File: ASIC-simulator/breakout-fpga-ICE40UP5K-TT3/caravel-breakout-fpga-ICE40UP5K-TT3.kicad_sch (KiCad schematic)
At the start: 65 parts, among them CON1 REF-182665-01, CON2 REF-182665-01, J15 USB4500-03-0-A_REVA, U1 AP2112K-3.3, U2 AP2112K-1.2, U2 ICE40UP5K-SG48ITR, U5 W25Q32JVSSIM, X1 20MHz

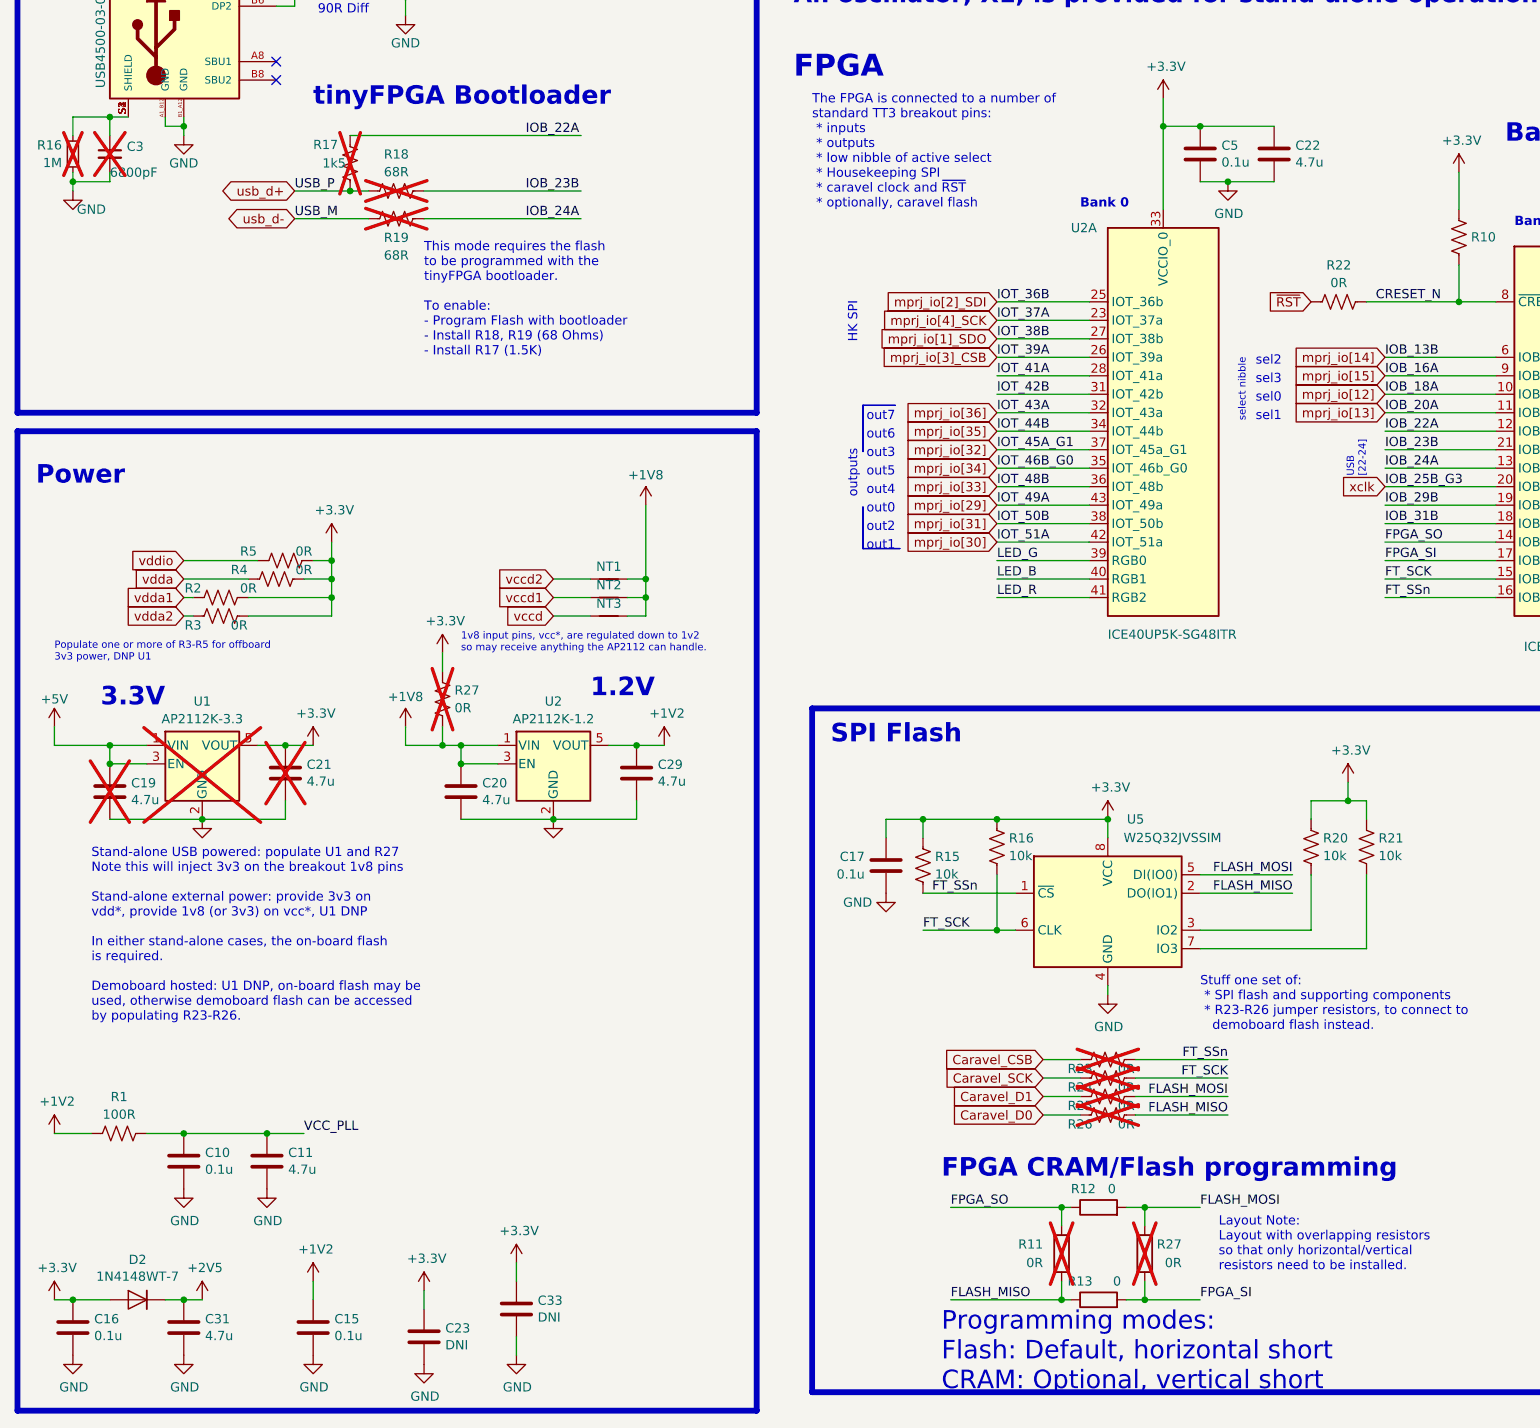
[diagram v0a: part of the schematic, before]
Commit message: ICE40UP5K TT3 breakout, BOM tweaks pre-PCBA first run
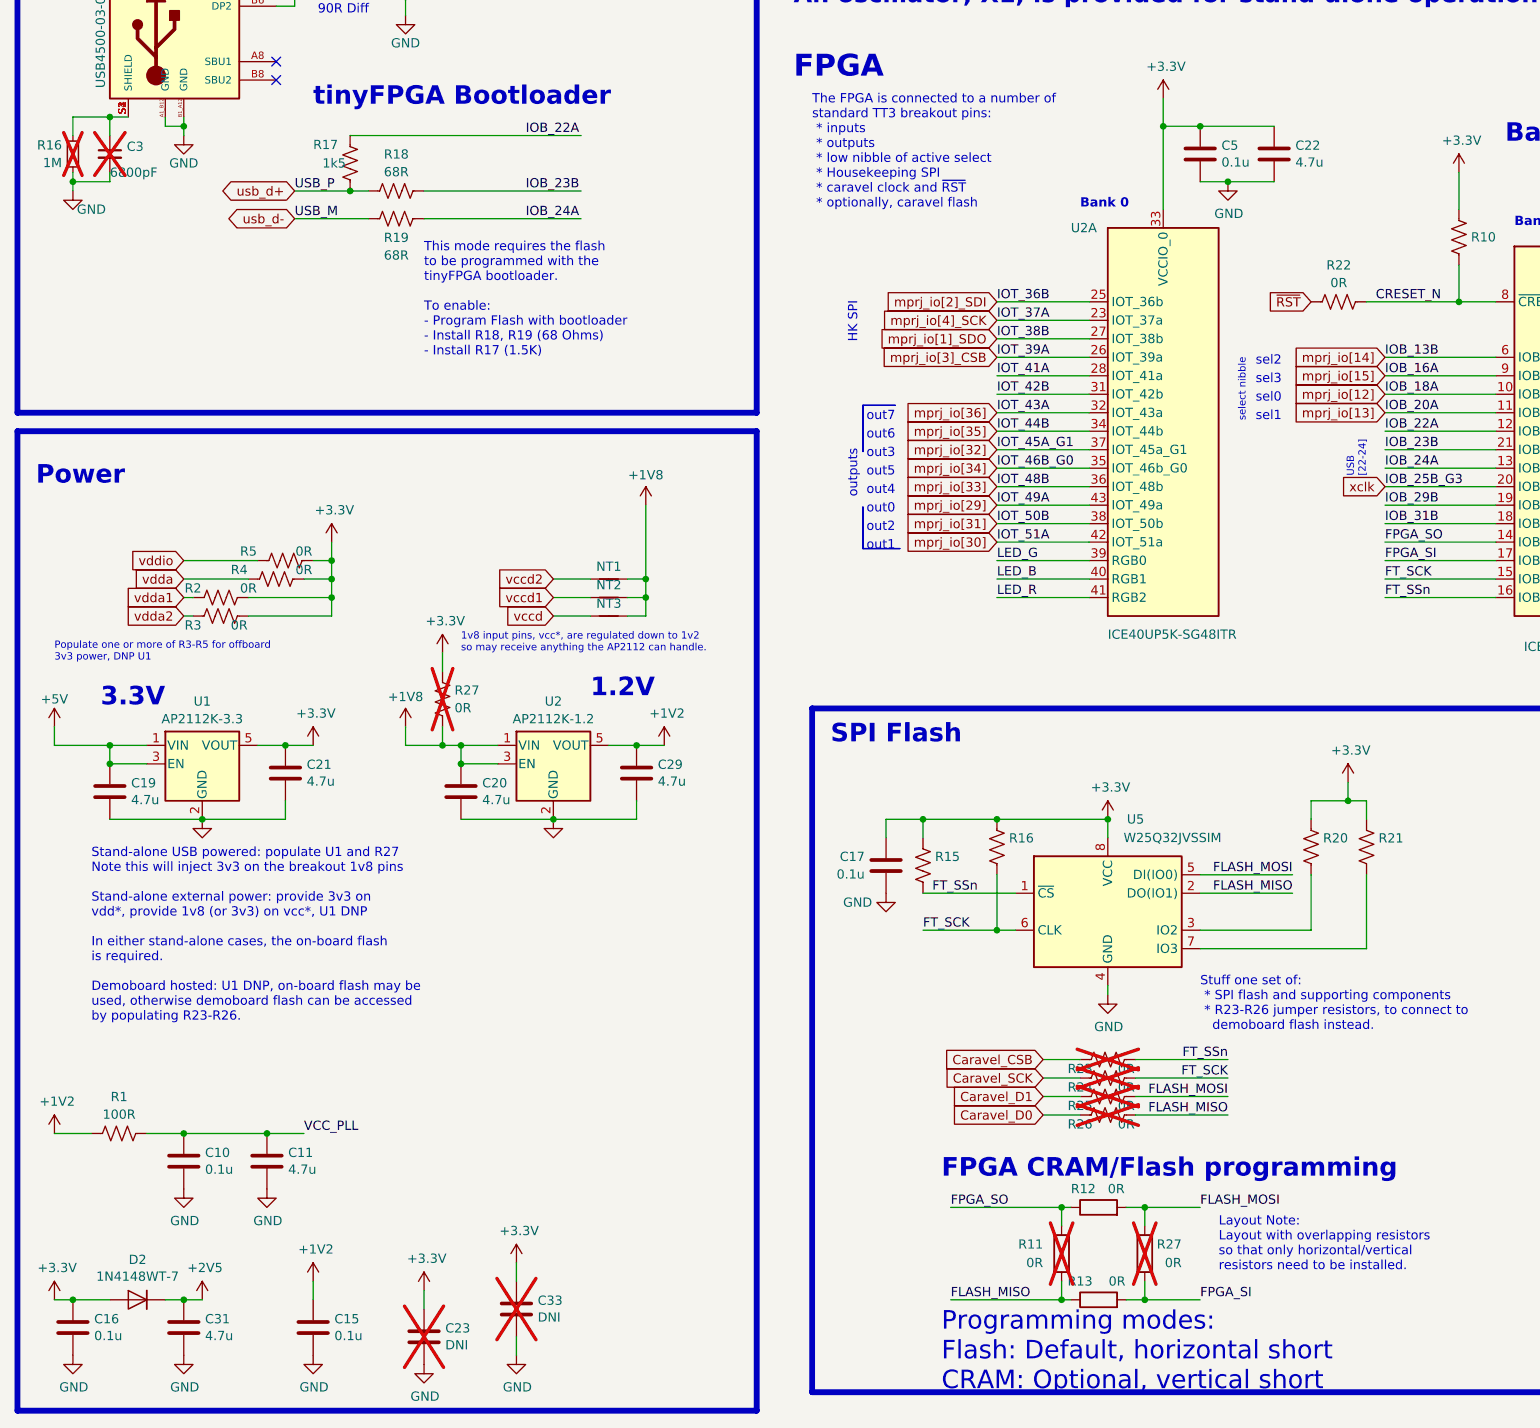
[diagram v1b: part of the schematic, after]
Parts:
- C10, C14, C15, C16, C17, C18, C36, C6: Characteristics (none) -> 0.1u 0402; MPN (none) -> CL05A104KA5NNNC
- C11, C20, C22, C29, C30, C31, C35: Characteristics (none) -> 4.7u 0603; MPN (none) -> CL10A475KQ8NNNC
- C19, C21: Characteristics (none) -> 4.7u 0603; MPN (none) -> CL10A475KQ8NNNC; Variant (none) -> USE_STANDALONE; now fitted
- C23, C33: now not fitted
- C3: DNP DNP -> (none); Variant (none) -> USB_SUPPORT
- C5: Characteristics (none) -> 0.1u 0402; MPN C1005X5R0J104K050BA -> CL05A104KA5NNNC
- CON1, CON2: MPN (none) -> M20-7812045; MPN_ALT (none) -> FH-00339
- D2: DigikeyPN (none) -> 1N4148WTDICT-ND; MPN (none) -> 1N4148WT-7; MPN_ALT (none) -> 1N4148XHE3-TP
- F1: Characteristics (none) -> Polyfuse 350mA Hold 0805; Variant (none) -> USB_SUPPORT
- FID1, FID2, FID3: now left out of the parts list
- J15: DigikeyPN (none) -> 2073-USB4500-03-0-ACT-ND
- R1: DigikeyPN (none) -> 311-100LRCT-ND; MPN (none) -> RC0402FR-07100RL; Manufacturer RC0402FR-07100RL -> (none); Vendor 311-100LRCT-ND -> (none)
- R10: DigikeyPN (none) -> 311-10.0KLRCT-ND; Display Value (none) -> 10k; MPN (none) -> RC0402FR-0710KL; Manufacturer ERJ-U02F1002X -> (none); Vendor 10-ERJ-U02F1002XCT-ND -> (none)
- R11: DigikeyPN (none) -> 311-2KLRCT-ND; MPN (none) -> RC0402FR-072KL; Manufacturer RC0402FR-072KL -> (none); Vendor 311-2KLRCT-ND -> (none)
- R11, R27: Characteristics (none) -> 0R JUMPER 0603; DigikeyPN (none) -> A106051CT-ND; Display Value (none) -> 0R; MPN (none) -> CRG0603ZR; Variant (none) -> PROG_CRAM
- R12, R13: value 0 -> 0R; Characteristics (none) -> 0R JUMPER 0603; DigikeyPN (none) -> A106051CT-ND; Display Value (none) -> 0R; MPN (none) -> CRG0603ZR; Variant (none) -> PROG_FLASH
- R15, R16, R20, R21: DigikeyPN (none) -> 311-10.0KLRCT-ND; Display Value (none) -> 10k; DisplayValue 10k -> (none); MPN (none) -> RC0402FR-0710KL; Manufacturer ERJ-U02F1002X -> (none); Vendor 10-ERJ-U02F1002XCT-ND -> (none)
- R16: Variant (none) -> USB_SUPPORT
- R17: DigikeyPN (none) -> 118-CR0603-FX-1501ELFDKR-ND; MPN (none) -> CR0603-FX-1501ELF; MPN_ALT (none) -> WR06X1501FTL; Variant (none) -> USB_SUPPORT; now fitted
- R18, R19: Characteristics (none) -> 68R 0603; DigikeyPN (none) -> CR0603-FX-68R0ELF; MPN (none) -> CR0603-FX-68R0ELF; MPN_ALT (none) -> WR06X68R0FTL; Variant (none) -> USB_SUPPORT; now fitted
- R2, R22, R27, R3, R4, R5: value R_0R_0603_JUMPER -> 0R; Characteristics (none) -> 0R JUMPER 0603; DigikeyPN (none) -> A106051CT-ND; MPN (none) -> CRG0603ZR; Manufacturer CRG0603ZR -> (none); Vendor A106051CT-ND -> (none)
- R20, R21: Characteristics (none) -> 5.1k 0402 1%; DigikeyPN (none) -> 13-AC0402FR-135K1LCT-ND; MPN AC0603FR-135K1L -> AC0402FR-135K1L; Variant (none) -> USB_SUPPORT
- R23, R24, R25, R26: value R_0R_0603_JUMPER -> 0R; Characteristics (none) -> 0R JUMPER 0603; DigikeyPN (none) -> A106051CT-ND; MPN (none) -> CRG0603ZR; Manufacturer CRG0603ZR -> (none); Variant (none) -> USE_DEMOBOARD; Vendor A106051CT-ND -> (none)
- U1: DigikeyPN (none) -> AP2112K-3.3TRG1DICT-ND; MPN (none) -> AP2112K-3.3TRG1; Variant (none) -> USE_STANDALONE; now fitted
- U2: DigikeyPN (none) -> 31-AP2112K-1.2TRG1CT-ND; MPN (none) -> AP2112K-1.2TRG1
- U2: DigikeyPN (none) -> 220-2212-1-ND; MPN (none) -> ICE40UP5K-SG48I
- U5: DigikeyPN (none) -> W25Q32JVSSIQ-ND; MPN (none) -> W25Q32JVSSIQ; Variant (none) -> USE_STANDALONE
- X1: DigikeyPN (none) -> 1923-830208220401CT-ND

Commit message: PCBA mods, new boot selector switch
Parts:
- added C15: 0.1u, Capacitor_SMD:C_0402_1005Metric, symbol UPduino_v3.0:Device_C
- added R28: R_10k_0402, Resistor_SMD:R_0402_1005Metric, symbol psypassives:R_10k_0402
- added R29: 1k5, Resistor_SMD:R_0603_1608Metric, symbol psypassives:R_0R_0603_JUMPER
- added SW1: 434121025816, TinyTapeout:434121025816, symbol Switch:SW_Push
- C3, F1, R16, R20, R21: Variant USB_SUPPORT -> USB
- R17, R18, R19: Variant USB_SUPPORT -> USB_COMM
- R2, R3, R4, R5: Variant (none) -> DEMOBOARD_DEPENDENT
- R23, R24, R25, R26: Variant USE_DEMOBOARD -> (none); now fitted
- R27: Variant (none) -> USE_STANDALONE
- X1: Variant (none) -> USE_STANDALONE; now fitted
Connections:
- net +3V3: now also R28.1
- net GND: now also C15.2, SW1.1
- net mprj_io[15]: no longer U2.9 (IOB_16a)
- new net: R28.2, R29.1, SW1.2
- new net BOOT: C15.1, R29.2, U2.9 (IOB_16a)
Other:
- note added: "Note: this is the TT123 breakout header arrangement. I *think* it was derived during the WLCSP days of the ICs but, regardless of the reason, it's a pretty awful pinout which has be reworked (breaking change) for TT4+."
- note added: "Populate one or more of R3-R5 for DEMOBOARD_DEPENDENT variant, in which case 3v3 power (U1) is DNP"
- note added: "TODO: rework these to disable flash stubs if no onboard, rather than interrupting lines to demoboard flash."
- note added: "The "Variant" field for components indicates whether to stuff for specific variations of board. * USB: usb connector and power * USB_COMM: TinyFPGA bootloader or other USB comms * USE_STANDALONE: board may self-powered and host its own flash, osc... * DEMOBOARD_DEPENDENT: board gets power and flash from (required) demoboard USB_COMM depends on USB. USE_STANDALONE and DEMOBOARD_DEPENDENT are mutua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"
- note added: "Variants"
- note removed: "Populate one or more of R3-R5 for offboard 3v3 power, DNP U1"
- note removed: "Stand-alone USB powered: populate U1 and R27 Note this will inject 3v3 on the breakout 1v8 pins Stand-alone external power: provide 3v3 on vdd*, provide 1v8 (or 3v3) on vcc*, U1 DNP In either stand-alone cases, the on-board flash is required. Demoboard hosted: U1 DNP, on-board flash may be used, otherwise demoboard flash can be accessed by populating R23-R26."
- moved on the sheet: C23, C33, D4, R11

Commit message: v1.2 ready for pcba
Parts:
- removed R25, R26, R27: 0R, Resistor_SMD:R_0603_1608Metric, symbol psypassives:R_0R_0603_JUMPER
- added NT4, NT5, NT6: NetTie_2, NetTie:NetTie-2_SMD_Pad0.5mm, symbol Device:NetTie_2
- added R25, R26, R30: R_10k_0402, Resistor_SMD:R_0402_1005Metric, symbol psypassives:R_10k_0402
- added R27, R32, R33, R34, R35, R36, R37, R38: R_100k_0402, Resistor_SMD:R_0402_1005Metric, symbol psypassives:R_100k_0402
- added R31: 0R, Resistor_SMD:R_0603_1608Metric, symbol psypassives:R_0R_0603_JUMPER
- C10, C14, C15, C16, C17, C18, C36, C5, C6: DigikeyPN (none) -> 1276-1043-1-ND
- C11, C19, C20, C21, C22, C29, C30, C31, C35: DigikeyPN (none) -> 1276-1044-1-ND; MPN CL10A475KQ8NNNC -> CL10A475KP8NNNC; MPN_ALT (none) -> GRT188R61C475KE13J
- C3: Characteristics (none) -> 6800p 0603
- CON1, CON2: Characteristics (none) -> 40 pos 100mil bottom + top; DigikeyPN (none) -> 952-3218-ND
- F1: DigikeyPN (none) -> 507-1812-1-ND
- J15: Characteristics (none) -> USB 2 Recept 16+8 Dummy
- R1: Characteristics (none) -> 100R 1% 0402
- R10, R15, R16, R20, R21, R28: Characteristics (none) -> 10k 0402
- R11: Characteristics (none) -> 2k 0402; now not fitted
- R16: Characteristics (none) -> 1M 0603
- R17: Characteristics (none) -> 1.5k 0603 1%; DigikeyPN 118-CR0603-FX-1501ELFDKR-ND -> 118-CR0603-FX-1501ELFCT-ND
- R23: Variant (none) -> DEMOBOARD_DEPENDENT
- R24: Variant (none) -> USE_STANDALONE
- R29: Characteristics (none) -> 1.5k 0603 1%; DigikeyPN 118-CR0603-FX-1501ELFDKR-ND -> 118-CR0603-FX-1501ELFCT-ND; Variant USB_COMM -> (none)
- R4, R5: Variant DEMOBOARD_DEPENDENT -> DEMOBOARD_BACKPOWERED
- SW1: Characteristics (none) -> NO MOM tactile switch
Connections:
- net +1V8: no longer C20.1, U2.1 (VIN), U2.3 (EN)
- net +3V3: now also C20.1, U2.1 (VIN), U2.3 (EN)
- net Caravel_D0: now also NT6.1
- net Caravel_D1: now also NT5.1
- net Caravel_SCK: now also NT4.1; no longer R24.1
- net FLASH_MISO: now also NT6.2
- net FLASH_MOSI: now also NT5.2
- net FT_SCK: now also NT4.2; no longer R24.2
- net FT_SSn: now also R24.2
- net GND: now also R25.2, R26.2, R27.2, R30.2, R32.2, R33.2, R34.2, R35.2, R36.2, R37.2, R38.2
- net mprj_io[12]: now also R26.1
- net mprj_io[13]: now also R25.1
- net mprj_io[14]: now also R30.1
- net mprj_io[21]: now also R33.1
- net mprj_io[22]: now also R37.1
- net mprj_io[23]: now also R38.1
- net mprj_io[24]: now also R34.1
- net mprj_io[25]: now also R36.1
- net mprj_io[26]: now also R32.1
- net mprj_io[27]: now also R27.1
- net mprj_io[28]: now also R35.1
- net mprj_io[3]_CSB: now also R24.1
- net xclk: now also R31.2; no longer CON1.38 (Pin_38)
- new net: CON1.38 (Pin_38), R31.1
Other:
- note added: "BOOT Switch"
- note added: "Flash ~{CS}"
- note added: "Flash ~{CS} variants: * DEMOBOARD_DEPENDENT: we use the flash on the demoboard, and populate R23 to get to it * STANDALONE: we use onboard flash, and populate R24 to provide external pin programming access"
- note added: "For this to work, the bootloader must be burned to the flash. Ideally, this will be burned prior to PCBA (it may then be updated via USB DFU) but in other cases it will be necessary to access the flash memory directly. SPI lines used by Caravel to access flash are reused here (SCK, D0 and D1). However, to avoid contention with the ~{CS} line in cases where flash is installed on both this PCB and 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"
- note added: "NO2 Bootloader"
- note added: "No PD avail on FPGA and demoboards either pull high or float. Need pull-downs here on select and inputs."
- note added: "ONE OF"
- note added: "Once the bootloader is installed, programming becomes a question of * holding the BOOT switch * plugging into computer USB * sending DFU to correct alternate Device shows up on USB as [1d50:6146] with four alternate endpoints 0: iCE40 bitstream 1: RISC-V firmware 2: Bootloader bitstream 3: Bootloader firmware"
- note added: "Populate one or more of R3-R5 for DEMOBOARD_DEPENDENT variant, in which case 3v3 power (U1) is DNP. May also populate if backpower to demoboard is desired."
- note added: "Programming"
- note added: "Programming modes: Flash: Default, R7/R8 short CRAM: Optional, R6/R9 short"
- note added: "Pulldowns"
- note added: "R23 or R24 (see Variant)"
- note added: "Stuff one set of: * SPI flash and supporting components, and R24 * R23 jumper resistors, to use demoboard flash instead."
- note added: "This breakout maps an ICE40UP5K (SG48ITR) FPGA to the TT 1,2 and 3 breakout board. It is designed to allow both stand-alone use and for interaction and support from the TT demo board. When used with the demo board, few components are required as the hosting PCB can provide power as well as the required serial flash. The bootloader may be used along with the USB interface to allow for simple updat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"
- note added: "no2bootloader"
- note added: "select bits"
- note added: "used to allow USB programming for users."
- note removed: "Populate one or more of R3-R5 for DEMOBOARD_DEPENDENT variant, in which case 3v3 power (U1) is DNP"
- note removed: "Programming modes: Flash: Default, horizontal short CRAM: Optional, vertical short"
- note removed: "Stuff one set of: * SPI flash and supporting components * R23-R26 jumper resistors, to connect to demoboard flash instead."
- note removed: "TODO: rework these to disable flash stubs if no onboard, rather than interrupting lines to demoboard flash."
- note removed: "This breakout maps an ICE40UP5K (SG48ITR) FPGA to the TT 1,2 and 3 breakout board. It is designed to allow both stand-alone use and for interaction and support from the TT demo board. When used with the demo board, few components are required as the hosting PCB can provide power as well as the required serial flash. The TinyFPGA bootloader may be used along with the USB interface, by populating R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"
- note removed: "sel3"
- note removed: "select nibble"
- note removed: "tinyFPGA Bootloader"
- moved on the sheet: C15, C18, C36, D4, FID1, FID2, FID3, R11, R12, R13, R23, R27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
